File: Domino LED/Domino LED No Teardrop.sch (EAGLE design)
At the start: 20 parts, among them J1 MH11-1

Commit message: Changed copyright
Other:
- note added: "The Domino Team may make changes to specifications and product"
- note added: "© 2014, The Domino Team All rights reserved."
- note removed: "Michel Stempin may make changes to specifications and product"
- note removed: "© 2014, Michel Stempin All rights reserved."
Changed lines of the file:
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@@
 <text x="302.26" y="12.7" size="0.8128" layer="94">Reference designs are provided "AS IS" and "WITH ALL FAULTS".</text>
 <text x="302.26" y="10.16" size="0.8128" layer="94">regarding this product, including but not limited to, any implied warranties of</text>
-<text x="302.26" y="6.35" size="0.8128" layer="94">Michel Stempin may make changes to specifications and product </text>
+<text x="302.26" y="6.35" size="0.8128" layer="94">The Domino Team may make changes to specifications and product </text>
 <text x="302.26" y="11.43" size="0.8128" layer="94">Global Marine Networks disclaims all other warranties express or implied, </text>
 <text x="302.26" y="8.89" size="0.8128" layer="94">merchantibility or fitness for any particular application.</text>
@@
 <text x="256.54" y="7.62" size="1.778" layer="94" align="center">Domino
 Qi</text>
-<text x="345.44" y="20.32" size="1.27" layer="94">© 2014, Michel Stempin
+<text x="345.44" y="20.32" size="1.27" layer="94">© 2014, The Domino Team
 All rights reserved.</text>
 <text x="379.222" y="5.334" size="1.778" layer="94">&gt;REV</text>

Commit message: ... and all the files I missed
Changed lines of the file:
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@@
 <attribute name="DATABASE" value="./../Common/BOM/Domino_DB.txt"/>
 <attribute name="DRAWN" value="M.STEMPIN"/>
-<attribute name="REV" value="A"/>
+<attribute name="REV" value="B"/>
 </attributes>
 <variantdefs>

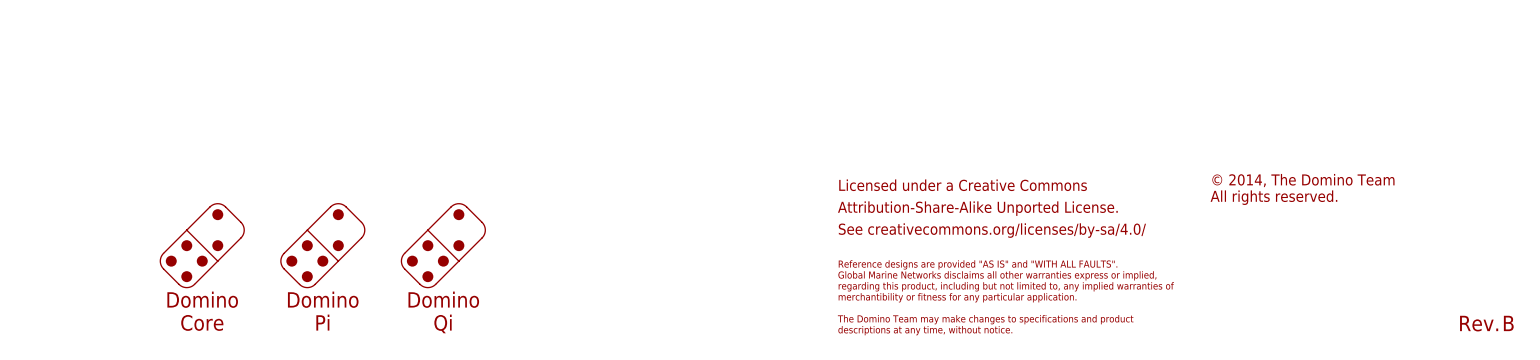
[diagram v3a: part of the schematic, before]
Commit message: Domino LED Rev. C: changed Logos
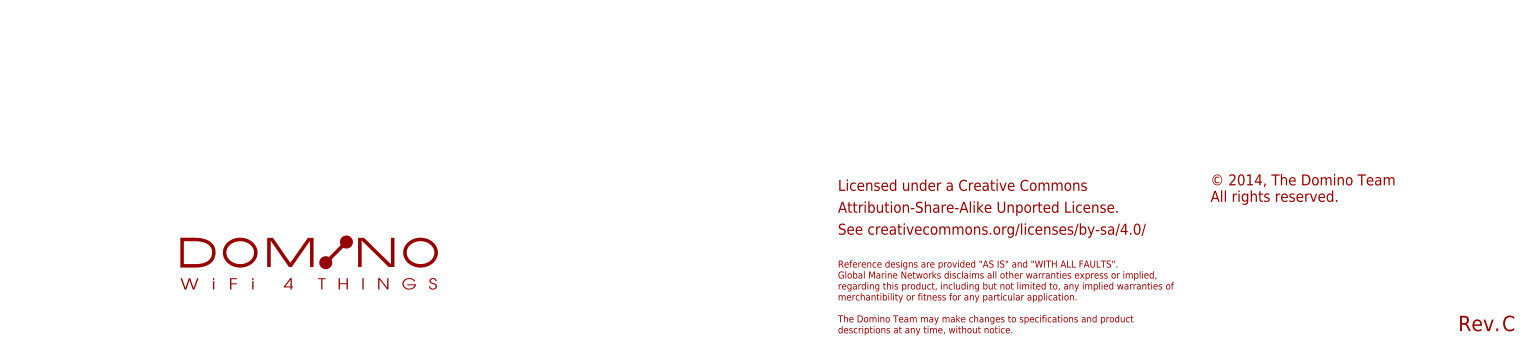
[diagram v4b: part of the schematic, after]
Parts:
- added U$4: DOMINO_LOGO, Domino:DOMINO_LOGO
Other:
- note removed: "Domino Core"
- note removed: "Domino Pi"
- note removed: "Domino Qi"
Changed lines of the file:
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@@
 <layer number="54" name="bGND_GNDA" color="1" fill="9" visible="no" active="no"/>
 <layer number="56" name="wert" color="7" fill="1" visible="no" active="no"/>
+<layer number="90" name="Modules" color="5" fill="1" visible="yes" active="yes"/>
 <layer number="91" name="Nets" color="2" fill="1" visible="yes" active="yes"/>
 <layer number="92" name="Busses" color="1" fill="1" visible="yes" active="yes"/>
@@
 <layer number="142" name="mbRestrict" color="7" fill="1" visible="no" active="no"/>
 <layer number="143" name="mvRestrict" color="7" fill="1" visible="no" active="no"/>
+<layer number="144" name="DrillLegend" color="7" fill="1" visible="yes" active="yes"/>
+<layer number="145" name="DrillLegend_01-16" color="2" fill="9" visible="yes" active="yes"/>
+<layer number="146" name="DrillLegend_01-20" color="3" fill="9" visible="yes" active="yes"/>
+<layer number="147" name="mMeasures" color="7" fill="1" visible="no" active="no"/>
 <layer number="148" name="mDocument" color="7" fill="1" visible="no" active="no"/>
 <layer number="149" name="mReference" color="7" fill="1" visible="no" active="no"/>
+<layer number="150" name="Pinout" color="7" fill="1" visible="yes" active="yes"/>
 <layer number="152" name="mbDocu" color="7" fill="1" visible="no" active="no"/>
 <layer number="191" name="mNets" color="7" fill="1" visible="no" active="no"/>
@@
 <layer number="195" name="mNames" color="7" fill="1" visible="no" active="no"/>
 <layer number="196" name="mValues" color="7" fill="1" visible="no" active="no"/>
+<layer number="200" name="Component_side" color="7" fill="1" visible="yes" active="yes"/>
+<layer number="201" name="Solder_side" color="7" fill="1" visible="yes" active="yes"/>
+<layer number="202" name="Silk_screen_CMP" color="7" fill="1" visible="yes" active="yes"/>
+<layer number="203" name="Silk_screen_SOL" color="7" fill="1" visible="yes" active="yes"/>
+<layer number="204" name="Solder_stop_mask_CMP" color="7" fill="1" visible="yes" active="yes"/>
+<layer number="205" name="Solder_stop_mask_SOL" color="7" fill="1" visible="yes" active="yes"/>
+<layer number="206" name="Cream_frame_CMP" color="7" fill="1" visible="yes" active="yes"/>
+<layer number="207" name="Cream_frame_SOL" color="7" fill="1" visible="yes" active="yes"/>
+<layer number="208" name="Drill_data" color="7" fill="1" visible="yes" active="yes"/>
+<layer number="209" name="Component_Assembly_CMP" color="7" fill="1" visible="yes" active="yes"/>
+<layer number="210" name="Component_Assembly_SOL" color="7" fill="1" visible="yes" active="yes"/>
+<layer number="211" name="Outline" color="7" fill="1" visible="yes" active="yes"/>
 <layer number="217" name="217bmp" color="18" fill="1" visible="no" active="no"/>
 <layer number="218" name="218bmp" color="19" fill="1" visible="no" active="no"/>
@@
 <attribute name="DATABASE" value="./../Common/BOM/Domino_DB.txt"/>
 <attribute name="DRAWN" value="M.STEMPIN"/>
-<attribute name="REV" value="B"/>
+<attribute name="REV" value="C"/>
 </attributes>
 <variantdefs>
@@
 <attribute name="TOL" value="5%"/>
 </part>
+<part name="U$4" library="Domino" deviceset="DOMINO_LOGO" device=""/>
 </parts>
 <sheets>
@@
 <text x="302.26" y="8.89" size="0.8128" layer="94">merchantibility or fitness for any particular application.</text>
 <text x="302.26" y="5.08" size="0.8128" layer="94">descriptions at any time, without notice.</text>
-<wire x1="238.079875" y1="14.341975" x2="240.77395" y2="17.036053125" width="0.1016" layer="94"/>
-<wire x1="240.77395" y1="17.036053125" x2="243.468028125" y2="19.730128125" width="0.1016" layer="94"/>
-<wire x1="243.468028125" y1="19.730128125" x2="245.264078125" y2="19.730128125" width="0.1016" layer="94" curve="-90"/>
-<wire x1="245.264078125" y1="19.730128125" x2="247.060128125" y2="17.934078125" width="0.1016" layer="94"/>
-<wire x1="247.060128125" y1="17.934078125" x2="247.060128125" y2="16.138028125" width="0.1016" layer="94" curve="-90"/>
-<wire x1="247.060128125" y1="16.138028125" x2="244.366053125" y2="13.44395" width="0.1016" layer="94"/>
-<wire x1="244.366053125" y1="13.44395" x2="241.671975" y2="10.749875" width="0.1016" layer="94"/>
-<wire x1="241.671975" y1="10.749875" x2="239.875925" y2="10.749875" width="0.1016" layer="94" curve="-90"/>
-<wire x1="239.875925" y1="10.749875" x2="238.079875" y2="12.545925" width="0.1016" layer="94"/>
-<wire x1="238.079875" y1="12.545925" x2="238.079875" y2="14.341975" width="0.1016" layer="94" curve="-90"/>
-<wire x1="240.77395" y1="17.036053125" x2="244.366053125" y2="13.44395" width="0.1016" layer="94"/>
-<circle x="238.9779" y="13.44395" radius="0.635" width="0" layer="94"/>
-<circle x="240.77395" y="15.240003125" radius="0.635" width="0" layer="94"/>
-<circle x="240.77395" y="11.6479" radius="0.635" width="0" layer="94"/>
-<circle x="242.57" y="13.44395" radius="0.635" width="0" layer="94"/>
-<circle x="244.366053125" y="15.24" radius="0.635" width="0" layer="94"/>
-<circle x="244.366053125" y="18.832103125" radius="0.635" width="0" layer="94"/>
-<wire x1="224.109875" y1="14.341975" x2="226.80395" y2="17.036053125" width="0.1016" layer="94"/>
-<wire x1="226.80395" y1="17.036053125" x2="229.498028125" y2="19.730128125" width="0.1016" layer="94"/>
-<wire x1="229.498028125" y1="19.730128125" x2="231.294078125" y2="19.730128125" width="0.1016" layer="94" curve="-90"/>
-<wire x1="231.294078125" y1="19.730128125" x2="233.090128125" y2="17.934078125" width="0.1016" layer="94"/>
-<wire x1="233.090128125" y1="17.934078125" x2="233.090128125" y2="16.138028125" width="0.1016" layer="94" curve="-90"/>
-<wire x1="233.090128125" y1="16.138028125" x2="230.396053125" y2="13.44395" width="0.1016" layer="94"/>
-<wire x1="230.396053125" y1="13.44395" x2="227.701975" y2="10.749875" width="0.1016" layer="94"/>
-<wire x1="227.701975" y1="10.749875" x2="225.905925" y2="10.749875" width="0.1016" layer="94" curve="-90"/>
-<wire x1="225.905925" y1="10.749875" x2="224.109875" y2="12.545925" width="0.1016" layer="94"/>
-<wire x1="224.109875" y1="12.545925" x2="224.109875" y2="14.341975" width="0.1016" layer="94" curve="-90"/>
-<wire x1="226.80395" y1="17.036053125" x2="230.396053125" y2="13.44395" width="0.1016" layer="94"/>
-<circle x="225.0079" y="13.44395" radius="0.635" width="0" layer="94"/>
-<circle x="226.80395" y="15.240003125" radius="0.635" width="0" layer="94"/>
-<circle x="226.80395" y="11.6479" radius="0.635" width="0" layer="94"/>
-<circle x="228.6" y="13.44395" radius="0.635" width="0" layer="94"/>
-<circle x="230.396053125" y="15.24" radius="0.635" width="0" layer="94"/>
-<circle x="230.396053125" y="18.832103125" radius="0.635" width="0" layer="94"/>
-<wire x1="252.049875" y1="14.341975" x2="254.74395" y2="17.036053125" width="0.1016" layer="94"/>
-<wire x1="254.74395" y1="17.036053125" x2="257.438028125" y2="19.730128125" width="0.1016" layer="94"/>
-<wire x1="257.438028125" y1="19.730128125" x2="259.234078125" y2="19.730128125" width="0.1016" layer="94" curve="-90"/>
-<wire x1="259.234078125" y1="19.730128125" x2="261.030128125" y2="17.934078125" width="0.1016" layer="94"/>
-<wire x1="261.030128125" y1="17.934078125" x2="261.030128125" y2="16.138028125" width="0.1016" layer="94" curve="-90"/>
-<wire x1="261.030128125" y1="16.138028125" x2="258.336053125" y2="13.44395" width="0.1016" layer="94"/>
-<wire x1="258.336053125" y1="13.44395" x2="255.641975" y2="10.749875" width="0.1016" layer="94"/>
-<wire x1="255.641975" y1="10.749875" x2="253.845925" y2="10.749875" width="0.1016" layer="94" curve="-90"/>
-<wire x1="253.845925" y1="10.749875" x2="252.049875" y2="12.545925" width="0.1016" layer="94"/>
-<wire x1="252.049875" y1="12.545925" x2="252.049875" y2="14.341975" width="0.1016" layer="94" curve="-90"/>
-<wire x1="254.74395" y1="17.036053125" x2="258.336053125" y2="13.44395" width="0.1016" layer="94"/>
-<circle x="252.9479" y="13.44395" radius="0.635" width="0" layer="94"/>
-<circle x="254.74395" y="15.240003125" radius="0.635" width="0" layer="94"/>
-<circle x="254.74395" y="11.6479" radius="0.635" width="0" layer="94"/>
-<circle x="256.54" y="13.44395" radius="0.635" width="0" layer="94"/>
-<circle x="258.336053125" y="15.24" radius="0.635" width="0" layer="94"/>
-<circle x="258.336053125" y="18.832103125" radius="0.635" width="0" layer="94"/>
-<text x="228.6" y="7.62" size="1.778" layer="94" align="center">Domino
-Core</text>
-<text x="242.57" y="7.62" size="1.778" layer="94" align="center">Domino
-Pi</text>
-<text x="256.54" y="7.62" size="1.778" layer="94" align="center">Domino
-Qi</text>
 <text x="345.44" y="20.32" size="1.27" layer="94">© 2014, The Domino Team
 All rights reserved.</text>
@@
 <attribute name="TOL" x="177.8" y="137.16" size="1.778" layer="96" display="off"/>
 </instance>
+<instance part="U$4" gate="G$1" x="226.06" y="12.7"/>
 </instances>
 <busses>

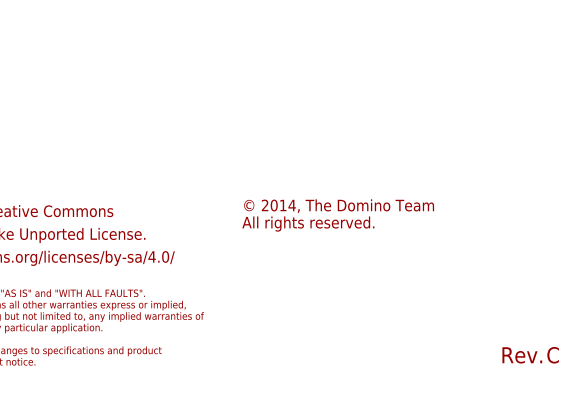
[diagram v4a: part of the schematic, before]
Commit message: Domino LED Rev. D: changed silkscreen font ratio to 20%
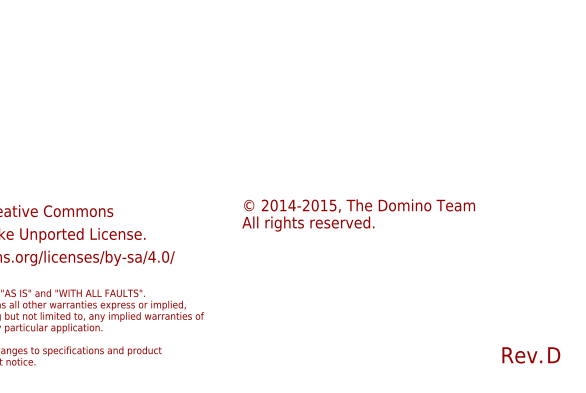
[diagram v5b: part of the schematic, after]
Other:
- note added: "© 2014-2015, The Domino Team All rights reserved."
- note removed: "© 2014, The Domino Team All rights reserved."
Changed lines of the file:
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@@
 <attribute name="DATABASE" value="./../Common/BOM/Domino_DB.txt"/>
 <attribute name="DRAWN" value="M.STEMPIN"/>
-<attribute name="REV" value="C"/>
+<attribute name="REV" value="D"/>
 </attributes>
 <variantdefs>
@@
 <text x="302.26" y="8.89" size="0.8128" layer="94">merchantibility or fitness for any particular application.</text>
 <text x="302.26" y="5.08" size="0.8128" layer="94">descriptions at any time, without notice.</text>
-<text x="345.44" y="20.32" size="1.27" layer="94">© 2014, The Domino Team
+<text x="345.44" y="20.32" size="1.27" layer="94">© 2014-2015, The Domino Team
 All rights reserved.</text>
 <text x="379.222" y="5.334" size="1.778" layer="94">&gt;REV</text>
